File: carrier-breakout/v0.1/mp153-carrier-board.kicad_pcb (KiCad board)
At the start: 2 copper layers, 87.2 x 87.4 mm, 99 parts, among them J1 USB-C_Receptacle_Molex_217179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, J10 3.5mm_Mono_Switched_sm, J11 3.5mm_Mono_Switched_sm, J12 3.5mm_Mono_Switched_sm, J13 3.5mm_Mono_Switched_sm, J2 Eurorack_Power_10pin_Shrouded, J5 3.5mm_Mono_Switched_sm, J9 3.5mm_Mono_Switched_sm, U1 TL072H, U11 TL072H, U12 TL072H, U13 AP6230xZ6, U14 AP2411SN, U3 FUSB302BMPX, U8 TL072H, U9 PCM3060PW

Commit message: Laying out board - WIP
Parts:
- removed C1, C2, C8: 100nF_0603_16V, 4ms_Capacitor:C_0603
- removed C81, C98: 10nF_0603_25V, 4ms_Capacitor:C_0603
- removed D1, D7: BAT54S, 4ms_Package_SOT:SOT23-3_PO132
- removed J5, J9: 3.5mm_Mono_Switched_sm, 4ms_Jack:EighthInch_PJ398SM
- removed POT1: 9mm_NoDet_100k_Knurled_Lined, 4ms_Potentiometer:Pot_9mm_Knurl_NoDet
- removed R13, R5: 47k_0603, 4ms_Resistor:R_0603
- removed R8: 100k_0603, 4ms_Resistor:R_0603
- removed U1: TL072H, 4ms_Package_SSOP:TSSOP-8_4.4x3mm_Pitch0.65mm
- added J6: Pins_02x40_P2.54mm_TH, Connector_PinHeader_2.54mm:PinHeader_2x40_P2.54mm_Vertical, F.Cu at (114.3, -58.0)
- added J7: Pins_02x40_P2.54mm_TH, Connector_PinHeader_2.54mm:PinHeader_2x40_P2.54mm_Vertical, F.Cu at (199.2, -58.0)
- added JP1: SolderJumper_2_Open, 4ms_SolderJumper:JUMPER_SMD_1x2_tiny, F.Cu at (223.6, 125.2)
- added JP10: SolderJumper_2_Open, 4ms_SolderJumper:JUMPER_SMD_1x2_tiny, F.Cu at (234.0, 112.2)
- added JP11: SolderJumper_2_Open, 4ms_SolderJumper:JUMPER_SMD_1x2_tiny, F.Cu at (144.5, 124.8)
- added JP12: SolderJumper_2_Open, 4ms_SolderJumper:JUMPER_SMD_1x2_tiny, F.Cu at (144.5, 126.9)
- added JP13: SolderJumper_2_Open, 4ms_SolderJumper:JUMPER_SMD_1x2_tiny, F.Cu at (144.5, 129.1)
- added JP14: SolderJumper_2_Open, 4ms_SolderJumper:JUMPER_SMD_1x2_tiny, F.Cu at (144.5, 131.2)
- added JP15: SolderJumper_2_Open, 4ms_SolderJumper:JUMPER_SMD_1x2_tiny, F.Cu at (144.5, 133.4)
- added JP2: SolderJumper_2_Open, 4ms_SolderJumper:JUMPER_SMD_1x2_tiny, F.Cu at (228.0, 121.2)
- added JP3: SolderJumper_2_Open, 4ms_SolderJumper:JUMPER_SMD_1x2_tiny, F.Cu at (216.3, 122.7)
- added JP4: SolderJumper_2_Open, 4ms_SolderJumper:JUMPER_SMD_1x2_tiny, F.Cu at (229.0, 119.7)
- added JP5: SolderJumper_2_Open, 4ms_SolderJumper:JUMPER_SMD_1x2_tiny, F.Cu at (231.0, 116.7)
- added JP6: SolderJumper_2_Open, 4ms_SolderJumper:JUMPER_SMD_1x2_tiny, F.Cu at (230.0, 118.2)
- added JP7: SolderJumper_2_Open, 4ms_SolderJumper:JUMPER_SMD_1x2_tiny, F.Cu at (217.1, 121.5)
- added JP8: SolderJumper_2_Open, 4ms_SolderJumper:JUMPER_SMD_1x2_tiny, F.Cu at (232.0, 115.2)
- added JP9: SolderJumper_2_Open, 4ms_SolderJumper:JUMPER_SMD_1x2_tiny, F.Cu at (233.0, 113.7)
- J3: footprint mp153-devboard:mp153-devboard-v0.1-sockets_B -> 4ms_Connector_Card:mp153-devboard-sockets_B
- J4: footprint mp153-devboard:mp153-devboard-v0.1-sockets_A -> 4ms_Connector_Card:mp153-devboard-sockets_A
- R1, R2: value 68Ω_0603 -> 10k_0402; footprint 4ms_Resistor:R_0603 -> 4ms_Resistor:R_0402
- R47, R48: value 4.7k_0402 -> 10k_0402
- moved J4 132.9 mm to (133.8, -11.3), turned to 0 degrees
- moved J3 113.0 mm to (183.8, -13.2), turned to 0 degrees
- moved R47 23.4 mm to (259.0, 121.0)
- moved R48 21.8 mm to (257.4, 118.6)
- moved R1 21.6 mm to (153.4, 101.3)
- moved R2 19.7 mm to (153.3, 106.7)
- moved C51 1.93 mm to (223.4, 127.4), turned to -90 degrees
- moved C49 1.63 mm to (221.3, 130.0)
- moved V1 1.63 mm to (221.0, 127.4)
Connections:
- net /USB_5V_ENABLE renamed /A57
- net /USB_HS_D+ renamed /A75
- net /USB_HS_D- renamed /A77
- net /USB_VBUS_JACK renamed /A71
- C41 pad 1: +3V3 -> /3v3_CODEC
- J3 pad B10: unconnected-(J3-PB7-PadB10) -> /B10
- J3 pad B12: unconnected-(J3-PD7-PadB12) -> /B12
- J3 pad B14: unconnected-(J3-PD1-PadB14) -> /B14
- J3 pad B16: unconnected-(J3-PE6-PadB16) -> /B16
- J3 pad B18: unconnected-(J3-PG15-PadB18) -> /B18
- J3 pad B2: /GATE1_IN -> /B2
- J3 pad B20: unconnected-(J3-PE12-PadB20) -> /B20
- J3 pad B22: unconnected-(J3-PE13-PadB22) -> /B22
- J3 pad B30: /CV_JACK1_ADC -> /ADC_16
- J3 pad B32: unconnected-(J3-PA3-PadB32) -> /ADC_15
- J3 pad B34: unconnected-(J3-PC3-PadB34) -> /ADC_13
- J3 pad B36: unconnected-(J3-PC2-PadB36) -> /ADC_12
- J3 pad B38: unconnected-(J3-PC1-PadB38) -> /ADC_11
- J3 pad B4: unconnected-(J3-PA9-PadB4) -> /B4
- J3 pad B40: unconnected-(J3-PA1-PadB40) -> /ADC_17
- J3 pad B42: unconnected-(J3-PB0-PadB42) -> /ADC_9
- J3 pad B44: unconnected-(J3-PA2-PadB44) -> /ADC_14
- J3 pad B46: unconnected-(J3-PB1-PadB46) -> /ADC_5
- J3 pad B48: unconnected-(J3-PC5-PadB48) -> /ADC_8
- J3 pad B50: unconnected-(J3-PC4-PadB50) -> /ADC_4
- J3 pad B52: unconnected-(J3-PC0-PadB52) -> /ADC_10
- J3 pad B54: unconnected-(J3-PA7-PadB54) -> /ADC_7
- J3 pad B56: unconnected-(J3-PA5-PadB56) -> /ADC_19
- J3 pad B58: /KNOB1_ADC -> /ADC_3
- J3 pad B6: unconnected-(J3-PB4-PadB6) -> /B6
- J3 pad B60: unconnected-(J3-PA4-PadB60) -> /ADC_18
- J3 pad B62: unconnected-(J3-PF11-PadB62) -> /ADC_2
- J3 pad B70: unconnected-(J3-PE2-PadB70) -> /B70
- J3 pad B72: unconnected-(J3-PG13-PadB72) -> /B72
- J3 pad B74: unconnected-(J3-PB8-PadB74) -> /B74
- J3 pad B76: unconnected-(J3-PB2-PadB76) -> /B76
- J3 pad B8: unconnected-(J3-PD0-PadB8) -> /B8
- J4 pad A1: unconnected-(J4-PB14-PadA1) -> /A1
- J4 pad A11: unconnected-(J4-PE4-PadA11) -> /A11
- J4 pad A13: unconnected-(J4-PC10-PadA13) -> /A13
- J4 pad A15: unconnected-(J4-PC11-PadA15) -> /A15
- J4 pad A17: unconnected-(J4-PD2-PadA17) -> /A17
- J4 pad A19: unconnected-(J4-PC12-PadA19) -> /A19
- J4 pad A3: unconnected-(J4-PA8-PadA3) -> /A3
- J4 pad A39: unconnected-(J4-NC-PadA39) -> /A39
- J4 pad A41: /CODEC_RESET -> /A41
- J4 pad A43: /SAI_MCLK -> /A43
- J4 pad A45: /SAI_FS -> /A45
- J4 pad A47: /SAI_SCK -> /A47
- J4 pad A49: /SAI_SD_A -> /A49
- J4 pad A5: unconnected-(J4-PB15-PadA5) -> /A5
- J4 pad A51: /SAI_SD_B -> /A51
- J4 pad A55: unconnected-(J4-PB10-PadA55) -> /A55
- J4 pad A59: /I2C6_SDA -> /A59
- J4 pad A61: /I2C6_SCL -> /A61
- J4 pad A63: /FUSB_INT -> /A63
- J4 pad A7: unconnected-(J4-PC8-PadA7) -> /A7
- J4 pad A9: unconnected-(J4-PC9-PadA9) -> /A9
- R1 pad 1: Net-(U1A--) -> /FUSB_I2C6_SDA
- R1 pad 2: /KNOB1_ADC -> /3V3_FUSB
- R2 pad 1: Net-(U1B--) -> /FUSB_I2C6_SCL
- R2 pad 2: /CV_JACK1_ADC -> /3V3_FUSB
- R47 pad 1: /I2C6_SCL -> /I2C6_SDA
- R47 pad 2: +3V3 -> /3v3_CODEC
- R48 pad 1: /I2C6_SDA -> /3v3_CODEC
- R48 pad 2: +3V3 -> /I2C6_SCL
- U3 pad 3: +5V -> /5V_FUSB
- U3 pad 4: +5V -> /5V_FUSB
- U3 pad 6: /I2C6_SCL -> /FUSB_I2C6_SCL
- U3 pad 7: /I2C6_SDA -> /FUSB_I2C6_SDA
- U9 pad 24: +5VA -> /5VA_CODEC
- U9 pad 7: +3V3 -> /3v3_CODEC
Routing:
- net +3V3: track 179.1 -> 59.6 mm, vias 6 -> 2
- net -12V: track 120.6 -> 53.8 mm, vias 9 -> 8
- net /CODEC_RESET: track 61.7 -> 0.00 mm, vias 2 -> 0
- net +12V: track 138.3 -> 79.1 mm, vias 9 -> 7
- net /GATE1_IN: track 56.0 -> 0.00 mm
- net /I2C6_SDA: track 52.7 -> 0.00 mm, vias 2 -> 0
- net /I2C6_SCL: track 52.1 -> 0.00 mm, vias 2 -> 0
- net /B76: track 0.00 -> 50.5 mm
- net /A77: track 17.0 -> 67.1 mm
- net /A1: track 0.00 -> 49.5 mm
- net /B74: track 0.00 -> 48.4 mm
- net /3v3_CODEC: track 0.00 -> 48.2 mm, vias 0 -> 3
- net /A75: track 16.9 -> 64.8 mm
- net /A3: track 0.00 -> 47.4 mm
- net Net-(D1-AK): track 46.7 -> 0.00 mm
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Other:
- board text removed: "CV IN"
- board text removed: "GATE IN"

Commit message: Organized breakoutheader silk
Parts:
- J6, J7: footprint Connector_PinHeader_2.54mm:PinHeader_2x40_P2.54mm_Vertical -> 4ms_Connector:Pins_2x40_P2.54mm_TH
- moved C11 293.2 mm to (-81.1, 36.9)
- moved C12 293.2 mm to (-74.3, 41.1)
- moved C3 293.2 mm to (-82.1, 36.9)
- moved C4 293.2 mm to (-80.9, 49.7)
- moved C5 293.2 mm to (-80.9, 57.9)
- moved C6 293.2 mm to (-75.6, 49.8)
- moved C7 293.2 mm to (-75.3, 57.9)
- moved C73 293.2 mm to (-79.6, 41.7)
- moved C74 293.2 mm to (-83.4, 41.9)
- moved D2 293.2 mm to (-86.4, 48.5)
- moved D3 293.2 mm to (-86.3, 60.2)
- moved J2 293.2 mm to (-93.0, 53.7)
- moved L5 293.2 mm to (-77.8, 38.1)
- moved R35 293.2 mm to (-83.6, 37.0)
- moved R36 293.2 mm to (-83.6, 36.0)
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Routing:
- net GND: track 799.2 -> 770.5 mm
- net GNDADC: track 72.0 -> 43.4 mm, vias 2 -> 0
- net VREF+: track 34.2 -> 43.8 mm, vias 2 -> 0
- net /A15: track 34.4 -> 28.3 mm
- net /A19: track 30.1 -> 24.0 mm
- net /A17: track 32.2 -> 26.2 mm
- net /A9: track 40.9 -> 34.8 mm
- net /A7: track 43.1 -> 37.0 mm
- net /A5: track 45.2 -> 39.1 mm
- net /A13: track 36.6 -> 30.5 mm
- net /A11: track 38.7 -> 32.6 mm
- net /A3: track 47.4 -> 41.3 mm
- net /A1: track 49.5 -> 43.5 mm
- net +5V: track 79.2 -> 75.0 mm
- net /B70: track 44.0 -> 47.7 mm
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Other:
- board size 87.2 x 87.4 mm -> 110 x 125 mm
- board text added: "A1 A3 A5 A7 A9 A11 A13 A15 A17 A19 A21 A23 A25 A27 A29 A31 A33 A35 A37 A39 A41 A43 A45 A47 A49 A51 A53 A55 A57 A59 A61 A63 A65 A65 A67 A69 A71 A73 A75 A77 A79"
- board text added: "A1 A3 A5 A7 A9 A11 A13 A15 A17 A19 A21 A23 A25 A27 A29 A31 A33 A35 A37 A39 A41 A43 A45 A47 A49 A51 A53 A55 A57 A59 A61 A63 A65 A67 A69 A71 A73 A75 A77 A79"
- board text added: "B2 B4 B6 B8 B10 B12 B14 B16 B18 B20 B22 B24 B26 B28 B30 B32 B34 B36 B38 B40 B42 B44 B46 B48 B50 B52 B54 B56 B58 B60 B62 B64 B66 B68 B70 B72 B74 B76 B78 B80"

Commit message: WIP - completeing traces
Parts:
- moved J2 156.9 mm to (18.0, -57.2), turned to -90 degrees
- moved D3 149.3 mm to (13.1, -51.3), turned to 180 degrees
- moved D2 148.0 mm to (22.8, -51.3), turned to 180 degrees
- moved C5 141.8 mm to (14.0, -47.5), turned to 180 degrees
- moved C4 141.4 mm to (21.9, -47.5), turned to 180 degrees
- moved C7 135.4 mm to (13.9, -43.9), turned to 0 degrees
- moved C6 134.9 mm to (21.5, -43.8), turned to 180 degrees
- moved C74 127.9 mm to (6.28, -49.3), turned to 0 degrees
- moved C73 122.2 mm to (2.40, -49.0), turned to 180 degrees
- moved U13 121.8 mm to (4.57, -46.6), turned to -90 degrees
- moved R35 121.4 mm to (6.43, -44.4), turned to 0 degrees
- moved R36 120.0 mm to (6.42, -43.4), turned to 180 degrees
- moved C3 118.9 mm to (4.91, -44.2), turned to -90 degrees
- moved C11 117.5 mm to (3.93, -44.2), turned to 90 degrees
- moved L5 114.7 mm to (0.69, -45.5), turned to 90 degrees
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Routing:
- net GND: track 770.5 -> 1004.9 mm, vias 23 -> 35
- net -12V: track 53.8 -> 165.6 mm, vias 8 -> 12
- net +12V: track 79.1 -> 186.8 mm, vias 7 -> 16
- net +5V: track 75.0 -> 172.5 mm, vias 5 -> 8
- net /A59: track 36.9 -> 120.3 mm, vias 0 -> 4
- net /A61: track 39.0 -> 122.0 mm, vias 0 -> 4
- net +3V3: track 60.3 -> 141.6 mm, vias 2 -> 3
- net /A41: track 18.3 -> 81.0 mm, vias 0 -> 2
- net /A49: track 26.0 -> 84.3 mm, vias 0 -> 2
- net /A71: track 79.2 -> 137.4 mm, vias 2 -> 4
- net /A43: track 19.6 -> 76.9 mm, vias 0 -> 2
- net /A47: track 23.9 -> 78.2 mm, vias 0 -> 2
- net /A45: track 21.7 -> 74.9 mm, vias 0 -> 2
- net /A77: track 67.7 -> 118.5 mm, vias 0 -> 2
- net /A51: track 28.2 -> 78.6 mm, vias 0 -> 2
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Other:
- board text removed: "A1 A3 A5 A7 A9 A11 A13 A15 A17 A19 A21 A23 A25 A27 A29 A31 A33 A35 A37 A39 A41 A43 A45 A47 A49 A51 A53 A55 A57 A59 A61 A63 A65 A65 A67 A69 A71 A73 A75 A77 A79"

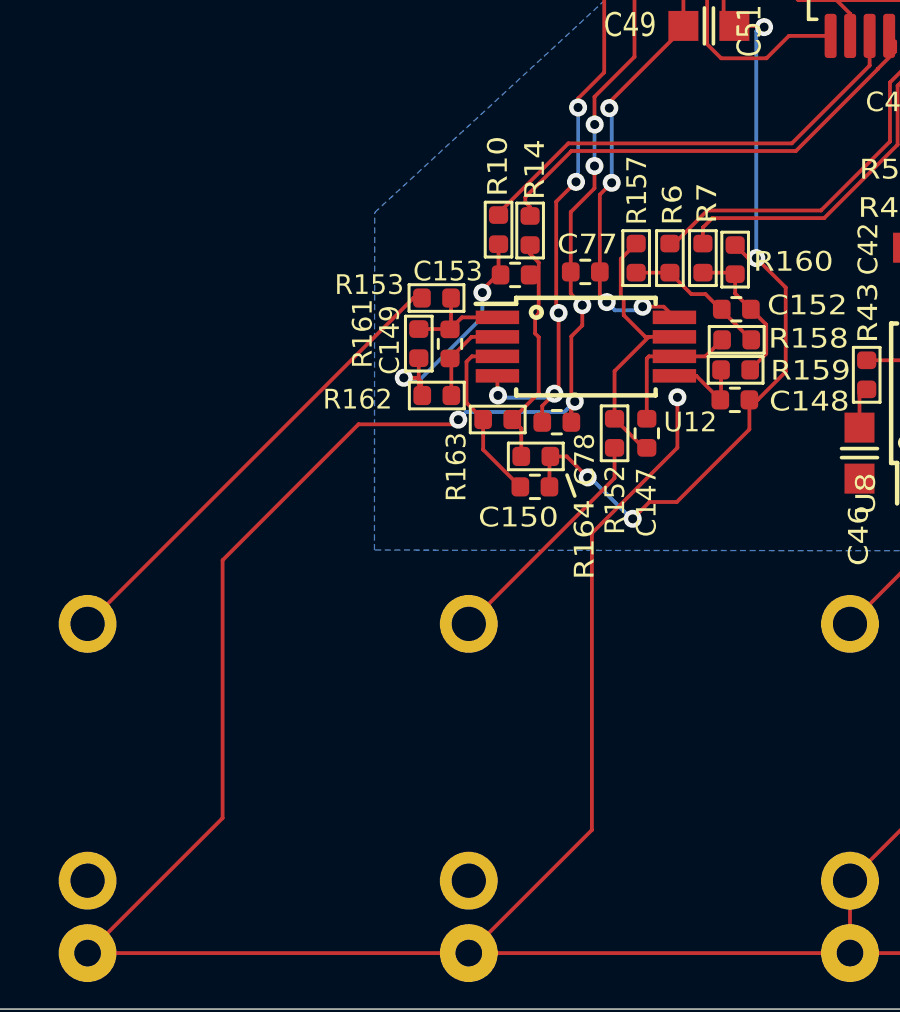
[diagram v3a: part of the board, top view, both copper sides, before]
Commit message: Begin fixing audio out section
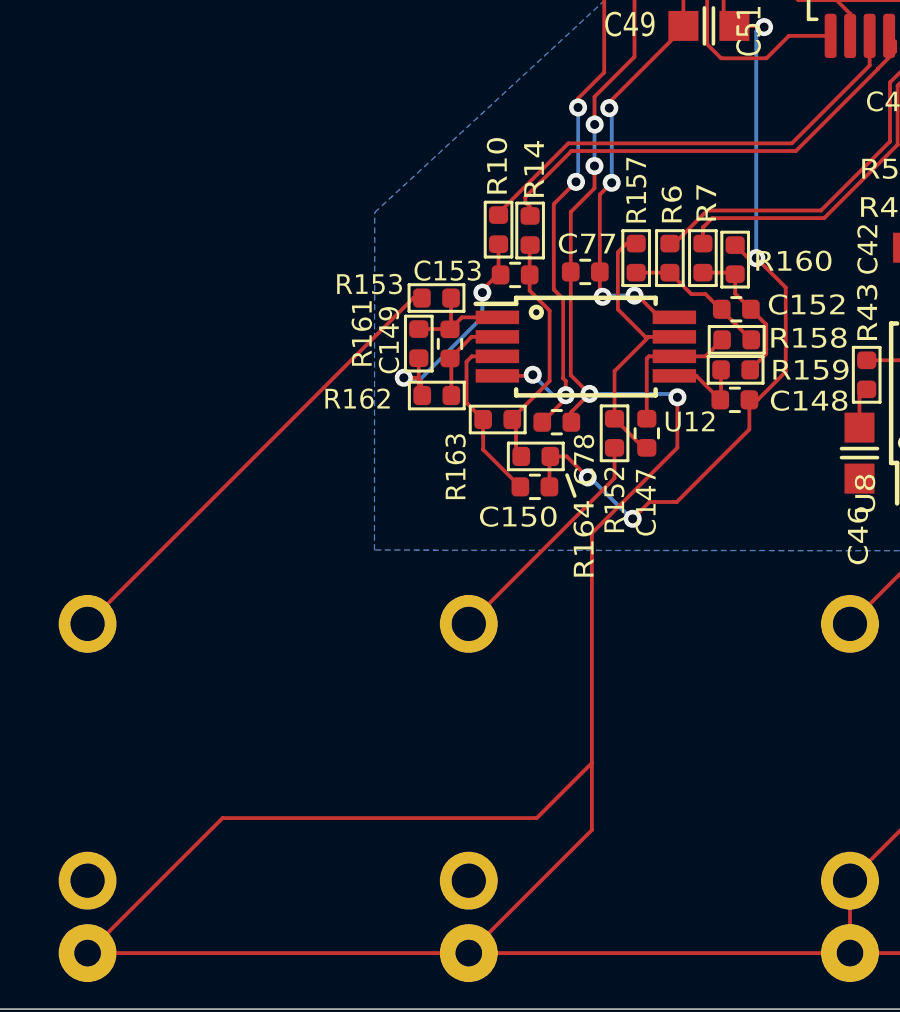
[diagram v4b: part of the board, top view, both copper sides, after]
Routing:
- net GND: track 1004.9 -> 998.0 mm, vias 35 -> 33
- net -12V: vias 12 -> 11

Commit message: Resolved ERC and DRC errors - warnings need to be reviewed. Cleaned up silk and cleaned up Audio out opamp section
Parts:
- moved R153 14.0 mm to (-16.9, 46.4), turned to 90 degrees
- moved R161 10.5 mm to (2.50, 33.9), turned to 180 degrees
- moved C150 10.3 mm to (-1.24, 34.8), turned to 0 degrees
- moved R164 10.2 mm to (-1.24, 33.9), turned to 0 degrees
- moved R160 9.96 mm to (-2.26, 44.6), turned to 0 degrees
- moved R162 9.95 mm to (1.10, 34.3), turned to 90 degrees
- moved R7 9.43 mm to (0.86, 46.5), turned to 180 degrees
- moved R163 9.15 mm to (0.16, 34.3), turned to 90 degrees
- moved C149 9.12 mm to (2.50, 34.8), turned to 180 degrees
- moved C152 8.18 mm to (-0.38, 45.5), turned to 180 degrees
- moved R6 8.13 mm to (1.49, 45.5), turned to 180 degrees
- moved C148 7.15 mm to (-2.26, 43.6), turned to 0 degrees
- moved R157 7.11 mm to (1.49, 44.6), turned to 180 degrees
- moved R10 6.57 mm to (2.03, 32.5)
- moved R159 6.33 mm to (-0.86, 44.1), turned to -90 degrees
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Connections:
- L1 pad 1: /A71 -> /USBSW_5V
- L1 pad 2: /USBSW_5V -> /A71
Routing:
- net Net-(C149-Pad1): track 3.79 -> 27.9 mm, vias 0 -> 2
- net GNDA: track 43.2 -> 21.5 mm, vias 4 -> 3
- net +12V: track 186.7 -> 204.3 mm, vias 16 -> 13
- net GNDADC: track 62.1 -> 74.9 mm
- net /AUDIO_OUT2: track 15.6 -> 2.83 mm
- net VREF+: track 59.0 -> 70.8 mm
- net /CODEC_OUT_L+: track 12.2 -> 21.1 mm
- net /CODEC_OUT_L-: track 12.5 -> 19.8 mm
- net /CODEC_OUT_R-: track 15.5 -> 8.84 mm
- net /CODEC_OUT_R+: track 15.6 -> 10.5 mm
- net Net-(C153-Pad2): track 7.97 -> 2.79 mm
- net GND: track 998.0 -> 1003.2 mm, vias 33 -> 30
- net Net-(C153-Pad1): track 7.93 -> 2.76 mm, vias 2 -> 0
- net -12V: track 165.6 -> 170.5 mm, vias 11 -> 7
- net Net-(U12A-+): track 6.02 -> 2.53 mm
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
